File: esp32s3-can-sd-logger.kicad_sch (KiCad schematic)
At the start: 0 parts

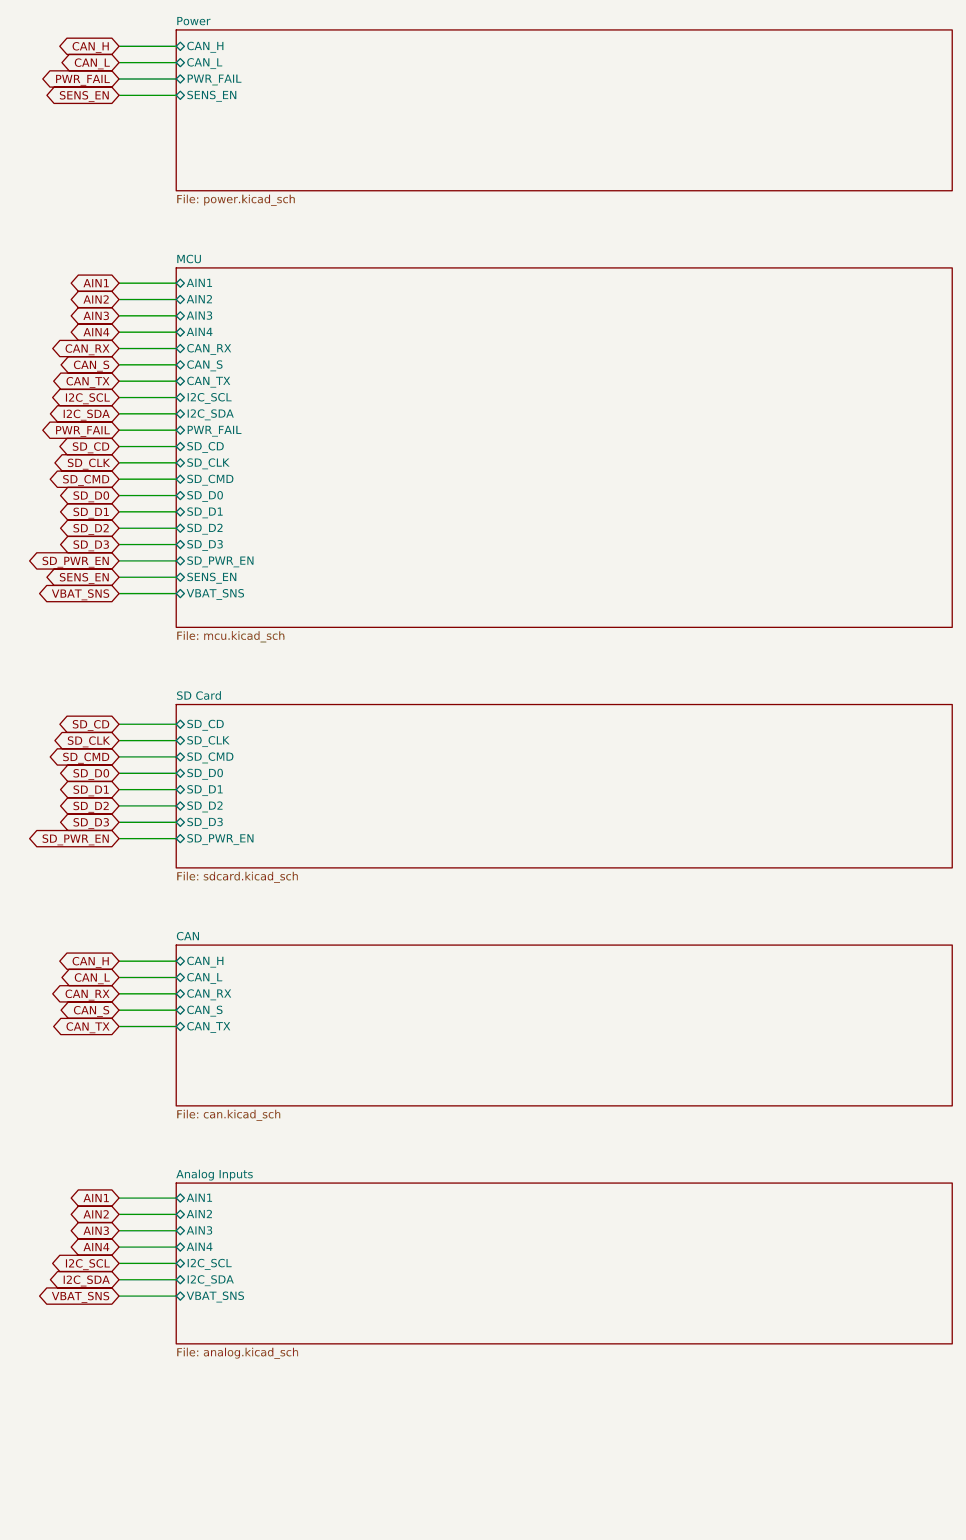
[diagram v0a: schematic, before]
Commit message: Re-scope the fork as a carrier board: no power section, differential analog, K-line
The shield idea does not survive measurement. Component courtyard on the
parent is 3052 mm2 over an 84 x 100 board -- 36% packing, not the 50% I had
been estimating -- and a DevKitC-1 is 63 x 25.5 = 1607 mm2. The parts alone
were 1.4x the whole dev board. So this is a carrier the dev board plugs into,
not a shield that fits on top of one.

Power section deleted entirely. It was 1746 mm2, 57% of the board, for two
rails the DevKitC-1 already makes from its USB-C. Gone: both LM5164 bucks and
everything around them, the LM74700 ideal diode, the reverse-battery FET, the
three electrolytic cans, the 12 V input, and the sensor-rail load switch.
Both rails are now inputs, taken up through the sockets -- which reverses the
earlier "feed 5 V only" rule, because there is no longer a second regulator
to parallel against.

Hold-up is a supercapacitor, not electrolytics. The first sizing was wrong:
energy goes as V-squared and the usable window at 5 V is 4.2 -> 3.6 V, so
2000 uF buys 12.5 ms, not the ~50 ms claimed. 0.5 F over the same window is
2.5 s, in less area than one of the 100 V cans it replaces. Low-ESR
cylindrical cells specifically -- coin EDLCs are 30-200 ohm and cannot source
120 mA at all.

Analog runs differentially. The board is grounded twice now, through the
sensor loom and through USB by way of a charger elsewhere in the car, and a
few hundred mV of chassis drop is 6% of a 0-5 V channel -- which makes the
0.1% dividers pointless. The correction has to be at the divider, not the
ADC, so the sensor ground comes back as a Kelvin wire through a matched
attenuator. Two ADS1115s, because one MUX only offers three channels against
a shared negative.

K-line added, discrete rather than an L9637D: that part's TXD threshold is
0.7*VCC = 3.5 V and a 3.3 V GPIO cannot meet it. Low-side 2N7002, clamped
22k/10k receiver, optional ISO 9141 tester pull-up on a jumper.

Pin map regrouped by boa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
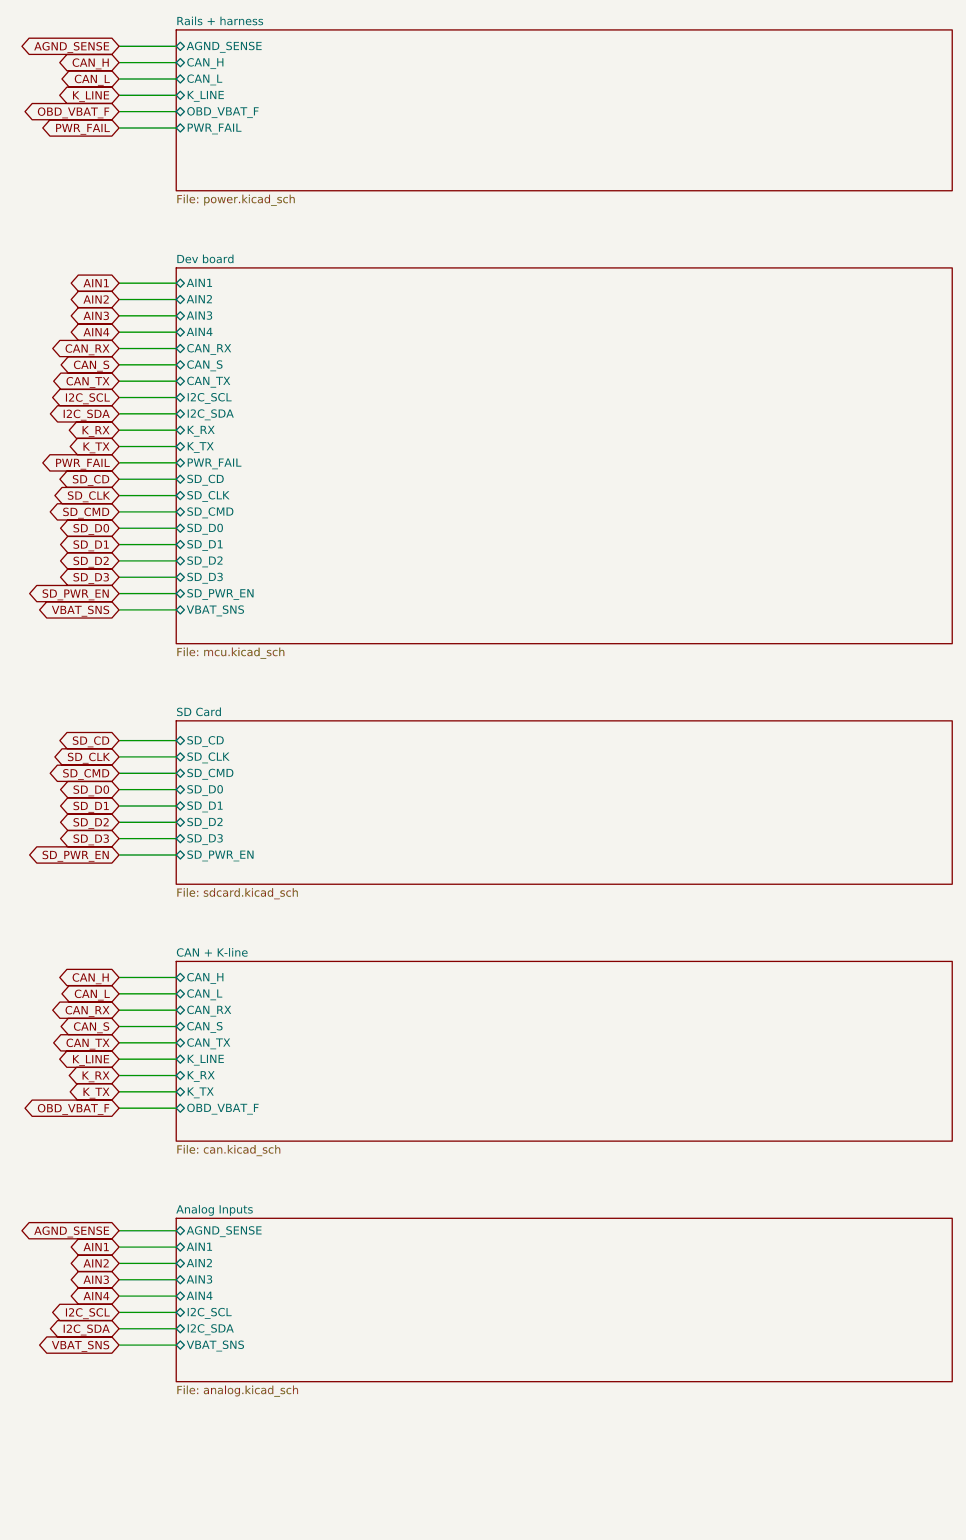
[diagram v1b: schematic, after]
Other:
- sheet CAN renamed CAN + K-line
- sheet MCU renamed Dev board
- sheet Power renamed Rails + harness
- sheet Analog Inputs ports: added AGND_SENSE; removed none
- sheet CAN + K-line ports: added K_LINE, K_RX, K_TX, OBD_VBAT_F; removed none
- sheet Dev board ports: added K_RX, K_TX; removed SENS_EN
- sheet Rails + harness ports: added AGND_SENSE, K_LINE, OBD_VBAT_F; removed SENS_EN

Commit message: Second CAN bus, single analog range, and three placement bugs the render caught
TWO CAN BUSES AT ONCE NEEDS A SECOND CONTROLLER. The ESP32-S3 has exactly
one TWAI peripheral. Two transceivers on it would give a bus you can pick at
runtime through the GPIO matrix, never two live at once, and the point of a
second bus is watching the powertrain and the body bus together. So the
second channel is an MCP2518FD on SPI (SOIC-14, KiCad ships the pin-compatible
MCP2517FD symbol) with its own 40 MHz crystal, its own TJA1051 -- same part
as CAN 1, so two positions on one BOM line -- choke, split termination and
clamps.

That cost five pins against two spare. The three came from dropping the
microSD to 1-bit SDMMC, which measurement says is free: the busiest case this
logger will see is ~128 kB/s against 1-bit's ~1500 kB/s, and bus width does
not touch the card's internal write stall, which is the only thing the
hold-up budget is actually sized around. The card keeps its D1/D2/D3
pull-ups because a card samples DAT3 at power-up and drops into SPI mode if
it finds it low -- they simply stop at the socket now.

Jumpers on the aux harness pins pick K-line or the second CAN pair, because
those two genuinely cannot share a wire: K-line idles at battery voltage and
a CAN transceiver biases its bus to 2.5 V. The clamps sit ahead of the
jumpers so the protection is the same either way, which also let the K-line
drop its own TVS. Default is K-line, which is what an R53 wants.

ANALOG DOWN TO ONE RANGE. The bypass and range-select jumpers are gone --
twelve jumpers and four resistors -- and every channel is a fixed 2.21/13.21
divider spanning 0-16 V, so a 5 V and a 12 V sensor both fit without
touching anything. Resolution was never the reason for a narrower range: a
5 V sensor lands at 0.836 V, which on a 16-bit ADS1115 is 6688 counts.

The real reason is the differential ground. A channel switched to 0-16 V
while the shared return attenuator stayed at the 0-5 V ratio subtracts
0.5769*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
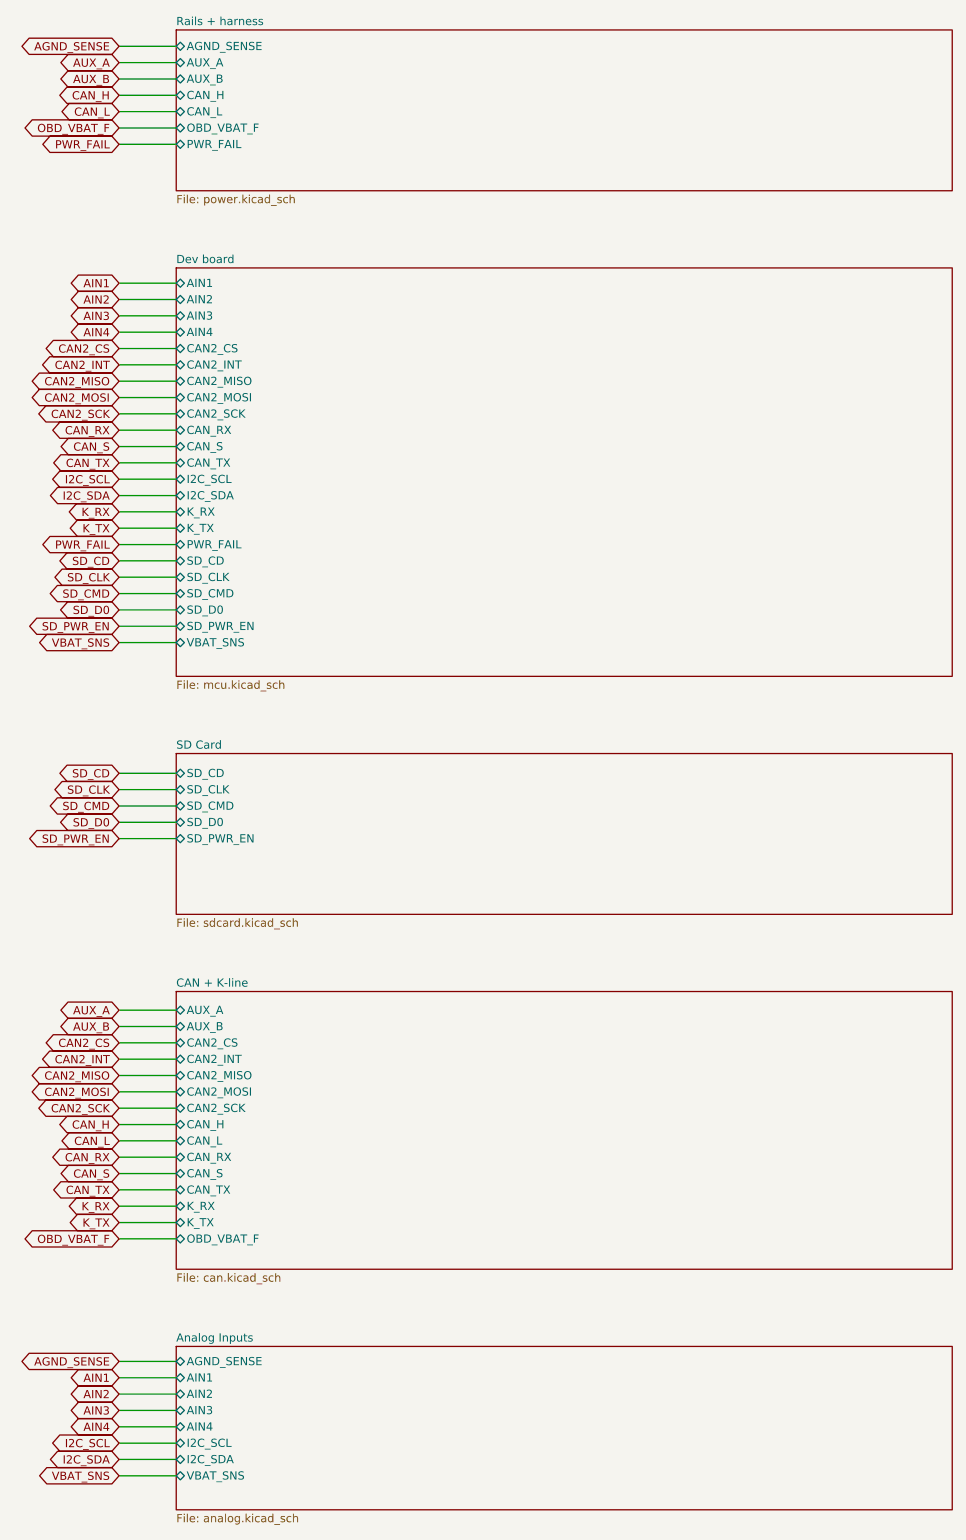
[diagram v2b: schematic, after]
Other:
- sheet CAN + K-line ports: added AUX_A, AUX_B, CAN2_CS, CAN2_INT, CAN2_MISO, CAN2_MOSI, CAN2_SCK; removed K_LINE
- sheet Dev board ports: added CAN2_CS, CAN2_INT, CAN2_MISO, CAN2_MOSI, CAN2_SCK; removed SD_D1, SD_D2, SD_D3
- sheet Rails + harness ports: added AUX_A, AUX_B; removed K_LINE
- sheet SD Card ports: added none; removed SD_D1, SD_D2, SD_D3
